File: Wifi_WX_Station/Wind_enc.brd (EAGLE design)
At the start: 25.5 x 25.5 mm, 9 parts, among them U1 AS5030

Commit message: updated BOM with all prices- As Checked in to BATCH PCB
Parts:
- +5V, GND, OUT: value LSP10 -> TPSOL; device solpad:LSP10 -> wifi_WX:TP_SOL
- moved +5V 0.64 mm to (14.0, 21.0)
- moved GND 0.64 mm to (14.0, 6.99)
- moved OUT 0.63 mm to (6.99, 14.0), turned to 0 degrees
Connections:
- net N$1: now also +5V.P$1; no longer +5V.MP
- net N$2: now also GND.P$1; no longer GND.MP
- net N$22: now also OUT.P$1; no longer OUT.MP
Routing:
- net N$1: track 22.4 -> 19.1 mm
- net N$23: track 8.21 -> 6.33 mm

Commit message: Revision B.1
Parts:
- moved GND 1.27 mm to (14.0, 8.26)
- moved +5V 1.27 mm to (14.0, 19.7)
- moved C1 1.27 mm to (19.7, 14.2)
- moved R6 1.27 mm to (10.2, 16.5)
- moved OUT 0.63 mm to (7.62, 14.0)
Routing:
- net N$1: track 19.1 -> 15.8 mm
- net N$2: track 32.0 -> 28.9 mm
- net N$22: track 8.90 -> 7.21 mm
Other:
- board size 25.5 x 25.5 mm -> 25.4 x 25.3 mm
- board text added: "+5V"
- board text added: "GND"
- board text added: "OUT"
- board text added: "Revision B.1"
- board text added: "Rv-Builders Products 2013"
- board text added: "Wind Dir Encoder WE27"
- board text removed: "."
- board text removed: "RV-Builders Products 2013"
- board text removed: "Wind Direction Encoder"

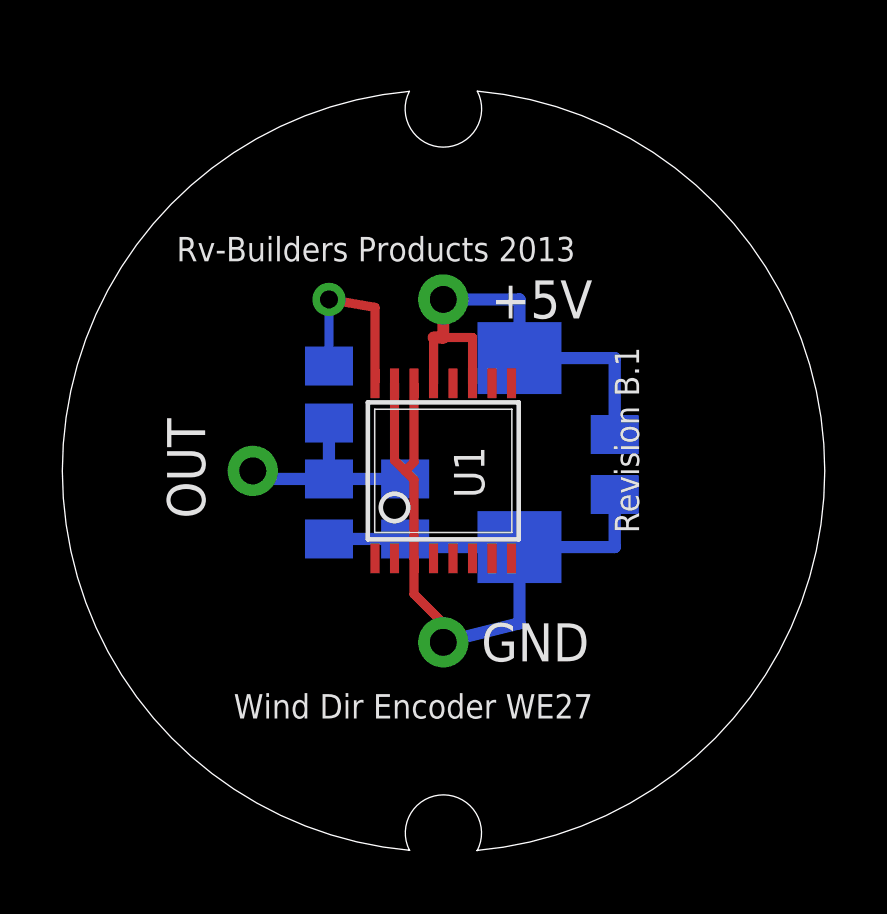
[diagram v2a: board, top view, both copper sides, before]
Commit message: 
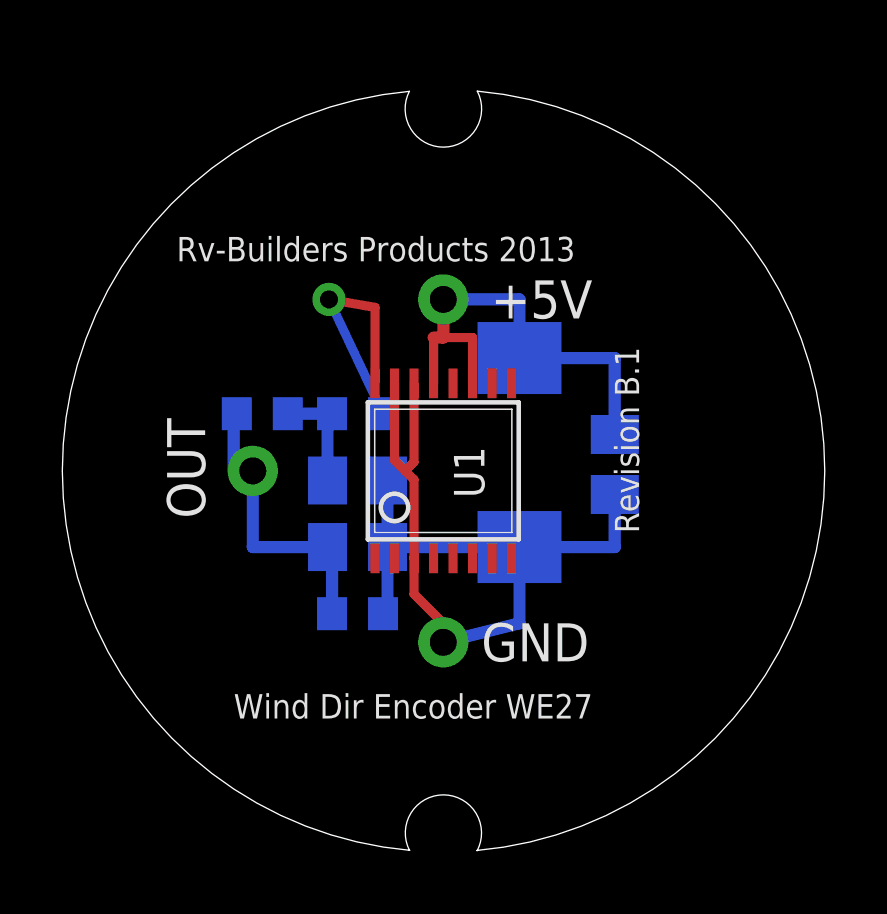
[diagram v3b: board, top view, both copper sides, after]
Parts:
- added R1: 6.8K, rcl:R0603
- added R2: 26.1k, rcl:R0603
- R6: value 6.8K -> 8.2K; device rcl:M0805 -> rcl:R0603
- moved C5 2.03 mm to (11.1, 11.4), turned to 180 degrees
- moved C2 1.35 mm to (11.1, 13.7), turned to 180 degrees
- moved R6 1.14 mm to (11.1, 15.9), turned to 180 degrees
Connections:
- new net N$3: C5.1, OUT.P$1, R1.1, R2.1
- net N$2: now also R2.2
- net N$22: now also R1.2; no longer C5.1, OUT.P$1
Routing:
- net N$3: track 0.00 -> 10.0 mm
- net N$22: track 7.21 -> 3.85 mm
- net N$2: track 28.9 -> 31.3 mm
- net N$23: track 6.33 -> 8.32 mm
